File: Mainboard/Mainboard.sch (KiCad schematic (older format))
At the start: 20 parts, among them J1 Conn_01x05, J2 Conn_02x08_Odd_Even, J3 Conn_02x06_Odd_Even, J4 Conn_02x06_Odd_Even, J5 Conn_02x02_Odd_Even, U1 ESP32-WROOM-32D, U2 ATxmega128A4U-AU

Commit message: Initial commit2
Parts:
- added D1, D2: D, Diode_SMD:D_0603_1608Metric, symbol Device:D
- added H1, H2, H3, H4: MountingHole_Pad, MountingHole:MountingHole_2.2mm_M2_DIN965_Pad, symbol Mechanical:MountingHole_Pad
- added Q1: BSS123, Package_TO_SOT_SMD:SOT-23, symbol Transistor_FET:BSS123
- added Q2: AO3401A, Package_TO_SOT_SMD:SOT-23, symbol Transistor_FET:AO3401A
- added R7: 100K, Resistor_SMD:R_0402_1005Metric, symbol Device:R
- U1: footprint RF_Module:ESP32-WROOM-32 -> HTV-mcu:ESP32-WROOM-32E
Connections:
- net RCON_BM_1: now also U2.29 (PE1); no longer U2.26 (PD6)
- net RCON_BM_2: now also U2.28 (PE0); no longer U2.27 (PD7)
- net VCC: now also Q2.2 (S)
- net GND renamed -BATT
- net -BATT: now also H2.1, H4.1, Q1.2 (S)
- new net: D1.2 (A), Q1.3 (D), Q2.1 (G), R7.1
- new net: D1.1 (K), D2.1 (K), H3.1
- new net +BATT: H1.1, Q2.3 (D), R7.2
- new net KEEPALIVE: Q1.1 (G)
- new net PWRBTN_IN: D2.2 (A)
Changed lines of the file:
@@
 F 0 "U1" H 5550 4731 50  0000 C CNN
 F 1 "ESP32-WROOM-32D" H 5550 4640 50  0000 C CNN
-F 2 "RF_Module:ESP32-WROOM-32" H 5550 1650 50  0001 C CNN
+F 2 "HTV-mcu:ESP32-WROOM-32E" H 5550 1650 50  0001 C CNN
 F 3 "https://www.espressif.com/sites/default/files/documentation/esp32-wroom-32d_esp32-wroom-32u_datasheet_en.pdf" H 5250 3200 50  0001 C CNN
 	1    5550 3150
@@
 Text Label 3300 5650 0    50   ~ 0
 LCON_BM_2
-Text Label 1900 6450 2    50   ~ 0
+Text Label 1900 5450 2    50   ~ 0
 RCON_BM_1
-Text Label 1900 6550 2    50   ~ 0
+Text Label 1900 5350 2    50   ~ 0
 RCON_BM_2
 NoConn ~ 1900 6150
@@
 Wire Wire Line
 	1100 3900 1450 3900
+$Comp
+L Mechanical:MountingHole_Pad H1
+U 1 1 6153DB61
+P 8700 800
+F 0 "H1" V 8937 803 50  0000 C CNN
+F 1 "MountingHole_Pad" V 8846 803 50  0000 C CNN
+F 2 "MountingHole:MountingHole_2.2mm_M2_DIN965_Pad" H 8700 800 50  0001 C CNN
+F 3 "~" H 8700 800 50  0001 C CNN
+	1    8700 800
+	0    -1   -1   0
+$EndComp
+$Comp
+L Mechanical:MountingHole_Pad H2
+U 1 1 6153E28C
+P 8700 1250
+F 0 "H2" V 8937 1253 50  0000 C CNN
+F 1 "MountingHole_Pad" V 8846 1253 50  0000 C CNN
+F 2 "MountingHole:MountingHole_2.2mm_M2_DIN965_Pad" H 8700 1250 50  0001 C CNN
+F 3 "~" H 8700 1250 50  0001 C CNN
+	1    8700 1250
+	0    -1   -1   0
+$EndComp
+$Comp
+L power:+BATT #PWR019
+U 1 1 61542794
+P 8800 800
+F 0 "#PWR019" H 8800 650 50  0001 C CNN
+F 1 "+BATT" V 8815 928 50  0000 L CNN
+F 2 "" H 8800 800 50  0001 C CNN
+F 3 "" H 8800 800 50  0001 C CNN
+	1    8800 800
+	0    1    1    0
+$EndComp
+$Comp
+L power:-BATT #PWR020
+U 1 1 61544599
+P 8800 1250
+F 0 "#PWR020" H 8800 1100 50  0001 C CNN
+F 1 "-BATT" V 8815 1378 50  0000 L CNN
+F 2 "" H 8800 1250 50  0001 C CNN
+F 3 "" H 8800 1250 50  0001 C CNN
+	1    8800 1250
+	0    1    1    0
+$EndComp
+$Comp
+L power:GND #PWR021
+U 1 1 61544EEA
+P 8800 1400
+F 0 "#PWR021" H 8800 1150 50  0001 C CNN
+F 1 "GND" H 8805 1227 50  0000 C CNN
+F 2 "" H 8800 1400 50  0001 C CNN
+F 3 "" H 8800 1400 50  0001 C CNN
+	1    8800 1400
+	1    0    0    -1
+$EndComp
+Wire Wire Line
+	8800 1250 8800 1400
+Connection ~ 8800 1250
+$Comp
+L Transistor_FET:AO3401A Q2
+U 1 1 6154E2C8
+P 10150 1000
+F 0 "Q2" V 10492 1000 50  0000 C CNN
+F 1 "AO3401A" V 10401 1000 50  0000 C CNN
+F 2 "Package_TO_SOT_SMD:SOT-23" H 10350 925 50  0001 L CIN
+F 3 "http://www.aosmd.com/pdfs/datasheet/AO3401A.pdf" H 10150 1000 50  0001 L CNN
+	1    10150 1000
+	0    -1   -1   0
+$EndComp
+$Comp
+L Device:R R7
+U 1 1 615519A2
+P 9800 1250
+F 0 "R7" V 9593 1250 50  0000 C CNN
+F 1 "100K" V 9684 1250 50  0000 C CNN
+F 2 "Resistor_SMD:R_0402_1005Metric" V 9730 1250 50  0001 C CNN
+F 3 "~" H 9800 1250 50  0001 C CNN
+	1    9800 1250
+	0    1    1    0
+$EndComp
+$Comp
+L power:+BATT #PWR022
+U 1 1 6155212E
+P 9550 900
+F 0 "#PWR022" H 9550 750 50  0001 C CNN
+F 1 "+BATT" H 9565 1073 50  0000 C CNN
+F 2 "" H 9550 900 50  0001 C CNN
+F 3 "" H 9550 900 50  0001 C CNN
+	1    9550 900
+	1    0    0    -1
+$EndComp
+Wire Wire Line
+	9950 900  9550 900
+$Comp
+L power:VCC #PWR025
+U 1 1 61557440
+P 10650 850
+F 0 "#PWR025" H 10650 700 50  0001 C CNN
+F 1 "VCC" H 10665 1023 50  0000 C CNN
+F 2 "" H 10650 850 50  0001 C CNN
+F 3 "" H 10650 850 50  0001 C CNN
+	1    10650 850
+	1    0    0    -1
+$EndComp
+$Comp
+L power:GND #PWR024
+U 1 1 6155AFB9
+P 10300 2650
+F 0 "#PWR024" H 10300 2400 50  0001 C CNN
+F 1 "GND" H 10305 2477 50  0000 C CNN
+F 2 "" H 10300 2650 50  0001 C CNN
+F 3 "" H 10300 2650 50  0001 C CNN
+	1    10300 2650
+	1    0    0    -1
+$EndComp
+$Comp
+L Mechanical:MountingHole_Pad H3
+U 1 1 6155E710
+P 10300 2100
+F 0 "H3" H 10200 2057 50  0000 R CNN
+F 1 "MountingHole_Pad" H 10200 2148 50  0000 R CNN
+F 2 "MountingHole:MountingHole_2.2mm_M2_DIN965_Pad" H 10300 2100 50  0001 C CNN
+F 3 "~" H 10300 2100 50  0001 C CNN
+	1    10300 2100
+	-1   0    0    1
+$EndComp
+$Comp
+L Mechanical:MountingHole_Pad H4
+U 1 1 6155D970
+P 10300 2400
+F 0 "H4" H 10400 2449 50  0000 L CNN
+F 1 "MountingHole_Pad" H 10400 2358 50  0000 L CNN
+F 2 "MountingHole:MountingHole_2.2mm_M2_DIN965_Pad" H 10300 2400 50  0001 C CNN
+F 3 "~" H 10300 2400 50  0001 C CNN
+	1    10300 2400
+	1    0    0    -1
+$EndComp
+Wire Wire Line
+	10300 2500 10300 2650
+Connection ~ 9550 900
+Wire Wire Line
+	9950 1250 10000 1250
+Wire Wire Line
+	10150 1250 10150 1200
+Wire Wire Line
+	9650 1250 9550 1250
+Wire Wire Line
+	9550 900  9550 1250
+Wire Wire Line
+	10650 850  10650 900
+Wire Wire Line
+	10650 900  10350 900
+Wire Wire Line
+	10300 2000 10300 1800
+Connection ~ 10300 1800
+$Comp
+L Device:D D2
+U 1 1 6158907E
+P 10450 1800
+F 0 "D2" H 10450 2017 50  0000 C CNN
+F 1 "D" H 10450 1926 50  0000 C CNN
+F 2 "Diode_SMD:D_0603_1608Metric" H 10450 1800 50  0001 C CNN
+F 3 "~" H 10450 1800 50  0001 C CNN
+	1    10450 1800
+	1    0    0    -1
+$EndComp
+$Comp
+L Device:D D1
+U 1 1 61588178
+P 10150 1800
+F 0 "D1" H 10150 1583 50  0000 C CNN
+F 1 "D" H 10150 1674 50  0000 C CNN
+F 2 "Diode_SMD:D_0603_1608Metric" H 10150 1800 50  0001 C CNN
+F 3 "~" H 10150 1800 50  0001 C CNN
+	1    10150 1800
+	-1   0    0    1
+$EndComp
+Wire Wire Line
+	10000 1800 10000 1250
+Connection ~ 10000 1250
+Wire Wire Line
+	10000 1250 10150 1250
+Wire Wire Line
+	9800 2050 9800 1800
+Wire Wire Line
+	9800 1800 10000 1800
+Connection ~ 10000 1800
+$Comp
+L power:GND #PWR023
+U 1 1 615C609F
+P 9800 2700
+F 0 "#PWR023" H 9800 2450 50  0001 C CNN
+F 1 "GND" H 9805 2527 50  0000 C CNN
+F 2 "" H 9800 2700 50  0001 C CNN
+F 3 "" H 9800 2700 50  0001 C CNN
+	1    9800 2700
+	1    0    0    -1
+$EndComp
+Wire Wire Line
+	9800 2700 9800 2450
+Text Label 10600 1800 0    50   ~ 0
+PWRBTN_IN
+Text Label 9500 2250 2    50   ~ 0
+KEEPALIVE
+$Comp
+L Transistor_FET:BSS123 Q1
+U 1 1 615E74CA
+P 9700 2250
+F 0 "Q1" H 9904 2296 50  0000 L CNN
+F 1 "BSS123" H 9904 2205 50  0000 L CNN
+F 2 "Package_TO_SOT_SMD:SOT-23" H 9900 2175 50  0001 L CIN
+F 3 "http://www.diodes.com/assets/Datasheets/ds30366.pdf" H 9700 2250 50  0001 L CNN
+	1    9700 2250
+	1    0    0    -1
+$EndComp
 $EndSCHEMATC

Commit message: power management
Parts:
- removed H1, H2, H3, H4: MountingHole_Pad, MountingHole:MountingHole_2.2mm_M2_DIN965_Pad, symbol Mechanical:MountingHole_Pad
- added C7: 1u, Capacitor_SMD:C_0402_1005Metric, symbol Device:C
- added C8: 2.2u, Capacitor_SMD:C_0402_1005Metric, symbol Device:C
- added C9: C, Capacitor_SMD:C_0402_1005Metric, symbol Device:C
- added J6, J9: Conn_01x04, Connector_PinHeader_2.54mm:PinHeader_1x04_P2.54mm_Vertical, symbol Connector_Generic:Conn_01x04
- added J7, J8: Conn_01x02, Connector_PinHeader_2.54mm:PinHeader_1x02_P2.54mm_Vertical, symbol Connector_Generic:Conn_01x02
- added R10: 1.5K, Resistor_SMD:R_0402_1005Metric, symbol Device:R
- added R11: 0.27, Resistor_SMD:R_1206_3216Metric, symbol Device:R
- added R8, R9: 33K, Resistor_SMD:R_0402_1005Metric, symbol Device:R
- added U3: LN1152, Package_TO_SOT_SMD:SOT-23-5, symbol HTV_power:LN1152
- added U4: TP4059, Package_TO_SOT_SMD:SOT-23-6, symbol HTV_power:TP4059
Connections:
- net +BATT: now also J7.2 (Pin_2), U4.3 (BAT)
- net -BATT: now also C7.2, C8.2, C9.2, J6.4 (Pin_4), J7.1 (Pin_1), J8.2 (Pin_2), J9.3 (Pin_3), J9.4 (Pin_4), R10.1, R9.1, U3.2 (GND), U4.2 (GND)
- net KEEPALIVE: now also U2.23 (PD3), U3.3 (CE)
- net PWRBTN_IN: now also U2.24 (PD4)
- net VCC: now also C8.1, U3.5 (VOUT); no longer Q2.2 (S)
- net BATT_MEAS: now reaches U2.1 (PA5)
- net BATT_MEAS: now also C9.1, R8.1, R9.2
- net BATT_NCHRG: now reaches U2.25 (PD5)
- net BATT_NCHRG: now also U4.1 (NCHRG), U4.5 (NSTBY)
- net USB_D-: now reaches U2.26 (PD6)
- net USB_D-: now also J6.2 (Pin_2)
- net USB_D+: now reaches U2.27 (PD7)
- net USB_D+: now also J6.3 (Pin_3)
- net at D1.1 (K), D2.1 (K): now also J8.1 (Pin_1)
- new net: J6.1 (Pin_1), R11.2
- new net: R10.2, U4.6 (PRG)
- new net +VSW: C7.1, J9.1 (Pin_1), J9.2 (Pin_2), Q2.2 (S), R8.2, U3.1 (VIN)
- new net USB_VCC: R11.1, U4.4 (VIN)
- no-connect marks 3 -> 9
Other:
- moved on the sheet: J2

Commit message: finetuning
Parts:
- added C10: 10u, Capacitor_SMD:C_0603_1608Metric, symbol Device:C
- added C11, C12, C13, C14: 100n, Capacitor_SMD:C_0402_1005Metric, symbol Device:C
- C9: value C -> 100n
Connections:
- net +BATT: now also C10.1
- net -BATT: now also C10.2, C11.1, C12.1, C13.1, C14.1
- net LCON_X: now also C14.2
- net LCON_Y: now also C13.2
- net RCON_X: now also C12.2
- net RCON_Y: now also C11.2
- no-connect marks 9 -> 19
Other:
- moved on the sheet: C1, R1, R2, R3, R4, U1

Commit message: fixing
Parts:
- removed U4: TP4059, Package_TO_SOT_SMD:SOT-23-6, symbol HTV_power:TP4059
- added C15: 10u, Capacitor_SMD:C_0603_1608Metric, symbol Device:C
- added C16: 22u, Capacitor_SMD:C_1206_3216Metric, symbol Device:C
- added C17: 10u, Capacitor_SMD:C_0402_1005Metric, symbol Device:C
- added U4: TP4056, Package_SO:HSOP-8-1EP_3.9x4.9mm_P1.27mm_EP2.41x3.1mm_ThermalVias, symbol HTV_power:TP4056
- C11, C12, C13, C14, C9: value 100n -> 100p
- R11: footprint Resistor_SMD:R_1206_3216Metric -> Resistor_SMD:R_0805_2012Metric
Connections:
- net +BATT: now also Q2.2 (S), U4.5 (BAT); no longer Q2.3 (D)
- net +VSW: now also Q2.3 (D), C16.1; no longer Q2.2 (S)
- net -BATT: now also R10.2, C15.2, C16.2, C17.2, U4.1 (TEMP), U4.3 (GND), U4.9 (GND); no longer R10.1
- net BATT_NCHRG: now also U4.6 (NSTDBY), U4.7 (NCHRG)
- net USB_VCC: now also C15.1, U4.4 (VIN), U4.8 (CE)
- net VCC: now also C17.1
- new net: R10.1, U4.2 (PROG)
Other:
- moved on the sheet: C9, R10, R8, R9

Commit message: Mainboard finished?
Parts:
- C8: value 2.2u -> 10u; footprint Capacitor_SMD:C_0402_1005Metric -> Capacitor_SMD:C_0805_2012Metric
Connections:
- net LCON_BM_A: now also U2.22 (PD2); no longer U2.20 (PD0)
- net LCON_BM_C: now also U2.20 (PD0); no longer U2.22 (PD2)
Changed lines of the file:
@@
 Text Label 5950 3150 0    50   ~ 0
 RCON_AUD
-Text Label 1350 5850 2    50   ~ 0
+Text Label 1350 6050 2    50   ~ 0
 LCON_BM_A
 Wire Wire Line
-	1900 5850 1350 5850
-Text Label 1850 5850 2    50   ~ 0
+	1900 6050 1350 6050
+Text Label 1850 6050 2    50   ~ 0
 RCON_BM_A
 Text Label 1850 5950 2    50   ~ 0
 RCON_BM_B
-Text Label 1850 6050 2    50   ~ 0
+Text Label 1850 5850 2    50   ~ 0
 RCON_BM_C
 Text Label 1350 5950 2    50   ~ 0
 LCON_BM_B
-Text Label 1350 6050 2    50   ~ 0
+Text Label 1350 5850 2    50   ~ 0
 LCON_BM_C
 Wire Wire Line
 	1350 5950 1900 5950
 Wire Wire Line
-	1900 6050 1350 6050
+	1900 5850 1350 5850
 Text Label 3300 5550 0    50   ~ 0
 LCON_BM_1
@@
 P 10750 3750
 F 0 "C8" H 10865 3796 50  0000 L CNN
-F 1 "2.2u" H 10865 3705 50  0000 L CNN
-F 2 "Capacitor_SMD:C_0402_1005Metric" H 10788 3600 50  0001 C CNN
+F 1 "10u" H 10865 3705 50  0000 L CNN
+F 2 "Capacitor_SMD:C_0805_2012Metric" H 10788 3600 50  0001 C CNN
 F 3 "~" H 10750 3750 50  0001 C CNN
 	1    10750 3750

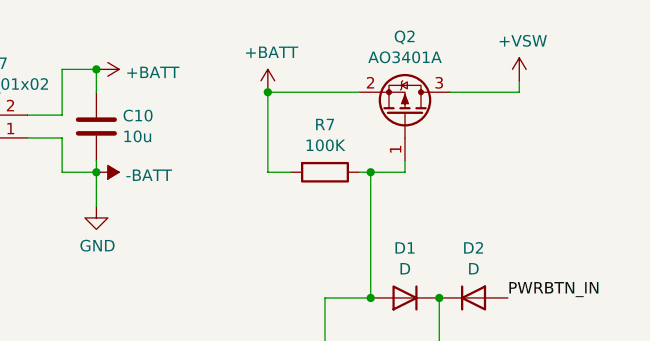
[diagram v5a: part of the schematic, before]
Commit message: more powerfull main pfet
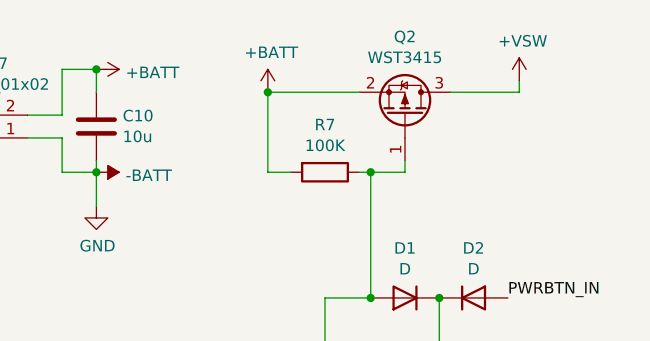
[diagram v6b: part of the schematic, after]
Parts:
- Q2: value AO3401A -> WST3415; footprint Package_TO_SOT_SMD:SOT-23 -> Package_TO_SOT_SMD:TSOT-23
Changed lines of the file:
@@
 P 10150 1000
 F 0 "Q2" V 10492 1000 50  0000 C CNN
-F 1 "AO3401A" V 10401 1000 50  0000 C CNN
-F 2 "Package_TO_SOT_SMD:SOT-23" H 10350 925 50  0001 L CIN
+F 1 "WST3415" V 10401 1000 50  0000 C CNN
+F 2 "Package_TO_SOT_SMD:TSOT-23" H 10350 925 50  0001 L CIN
 F 3 "http://www.aosmd.com/pdfs/datasheet/AO3401A.pdf" H 10150 1000 50  0001 L CNN
 	1    10150 1000
